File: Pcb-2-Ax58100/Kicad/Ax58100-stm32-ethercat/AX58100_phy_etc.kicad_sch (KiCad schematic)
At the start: 46 parts, among them U3 AMS1117-1.2

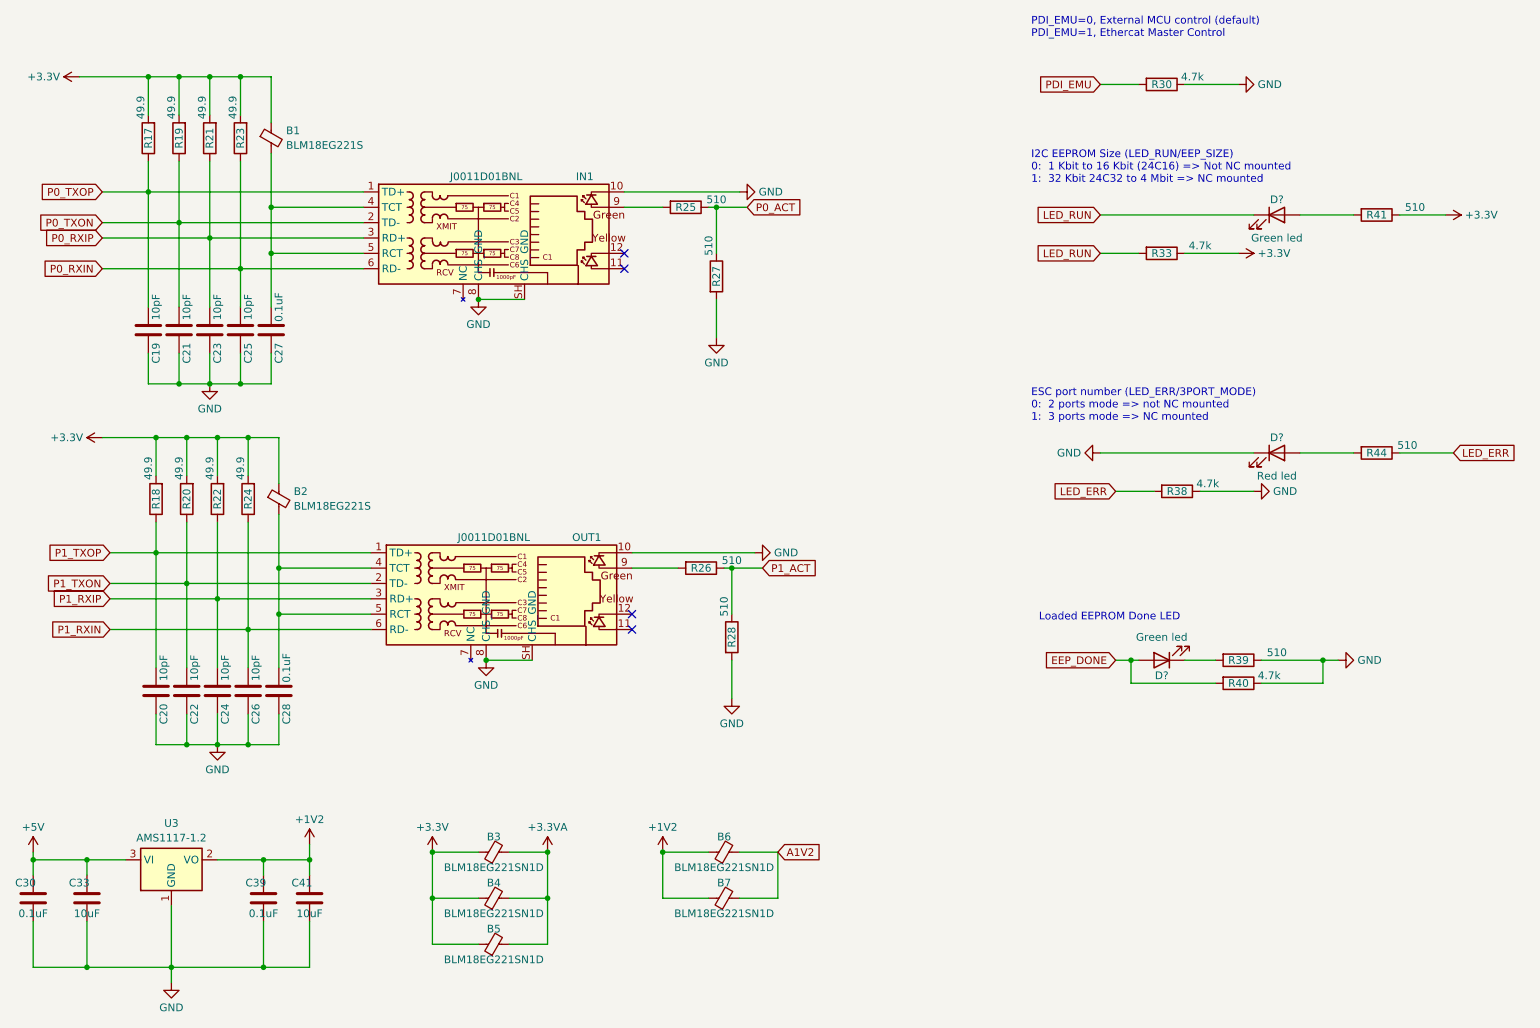
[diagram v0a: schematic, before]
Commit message: Geographic annotation on pcb 2
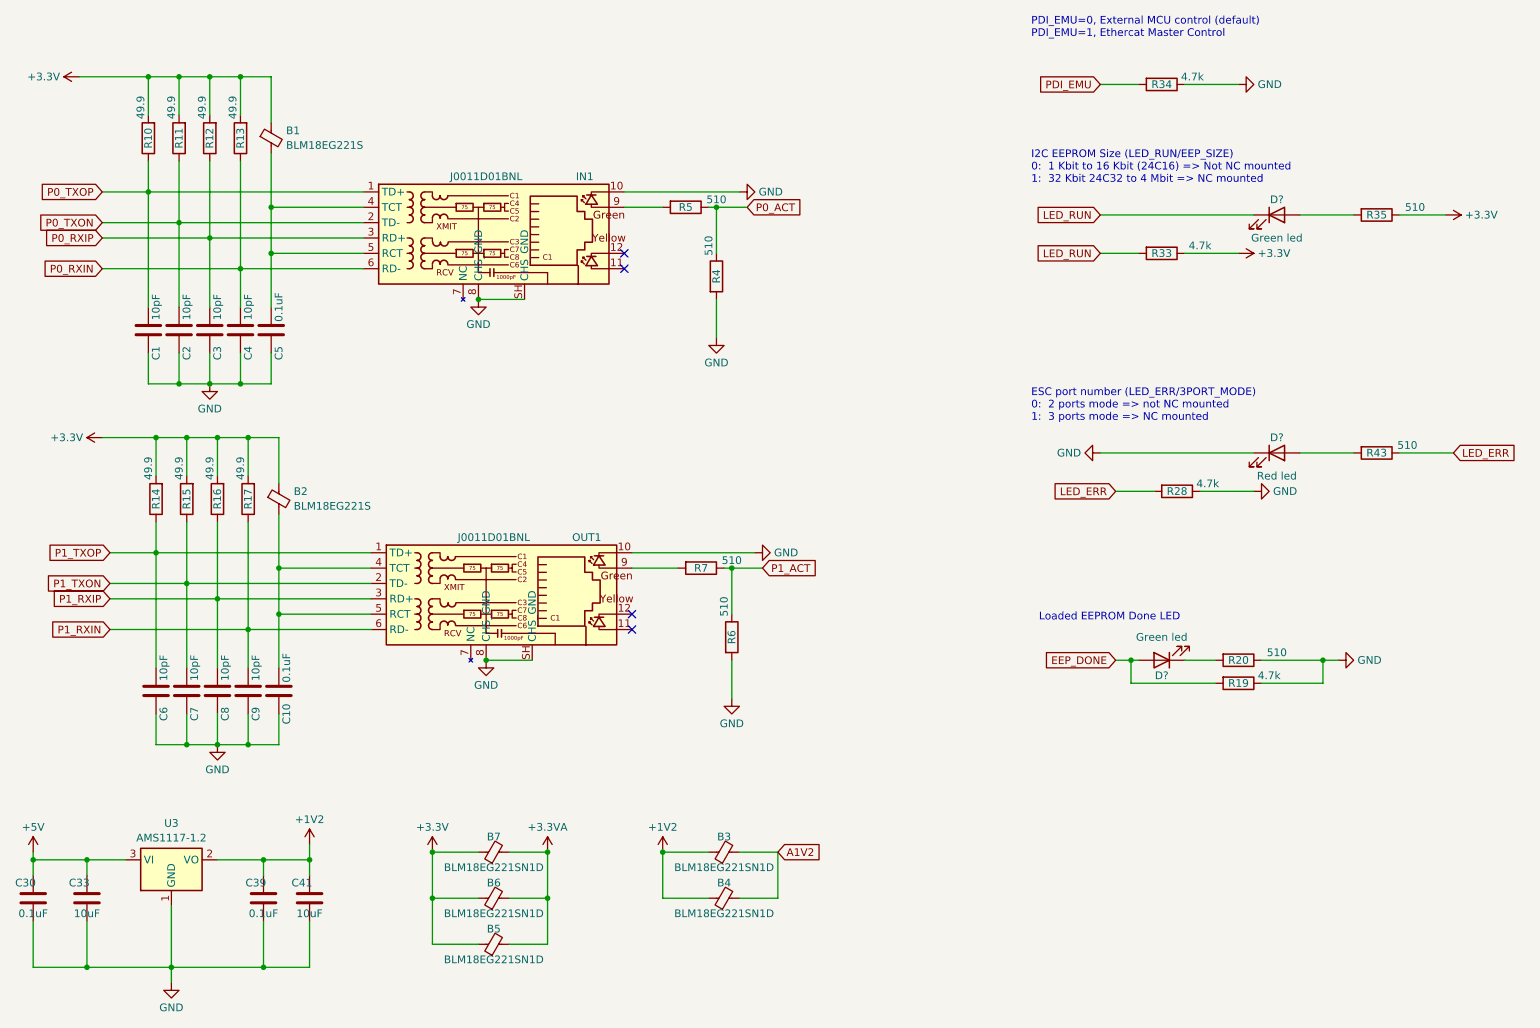
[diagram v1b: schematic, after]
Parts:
- renumbered B6 to B3, B7 to B4, B4 to B6, B3 to B7, C19 to C1, C28 to C10, C21 to C2, C23 to C3, C25 to C4, C27 to C5, C20 to C6, C22 to C7, C24 to C8, C26 to C9, R17 to R10, R19 to R11, R21 to R12, R23 to R13, R18 to R14, R20 to R15, R22 to R16, R24 to R17, R40 to R19, R39 to R20, R38 to R28, R30 to R34, R41 to R35, R27 to R4, R44 to R43, R25 to R5, R28 to R6, R26 to R7
